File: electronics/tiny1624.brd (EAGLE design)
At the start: 22.9 x 16.3 mm, 7 parts, among them U1 ATTINY1624

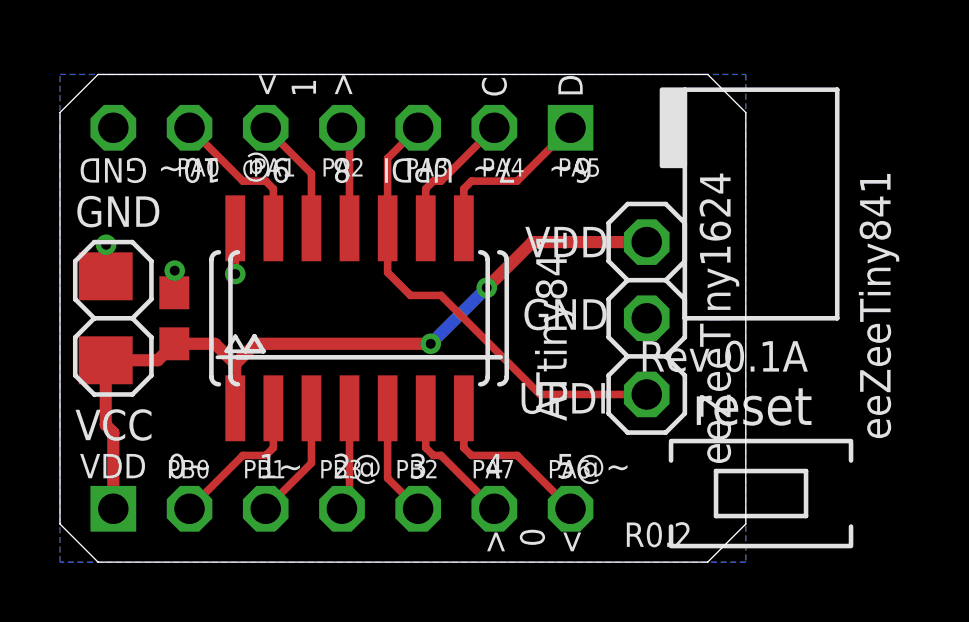
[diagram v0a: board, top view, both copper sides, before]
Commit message: changed silk to _24
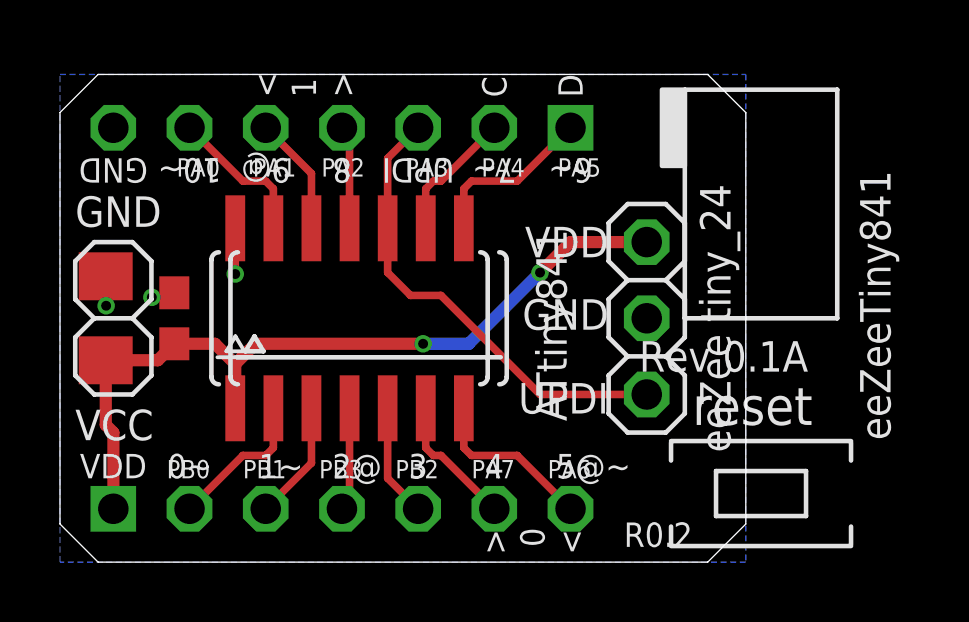
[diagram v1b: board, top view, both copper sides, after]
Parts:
- moved U$1 0.13 mm to (6.48, 6.60)
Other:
- board text added: "eeZee tiny_24"
- board text removed: "eeZeeTiny1624"
